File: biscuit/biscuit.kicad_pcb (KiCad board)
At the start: 2 copper layers, 45.7 x 45.7 mm, 47 parts, among them IC1 ATMEGA328-A, P1 D_IN, P2 PWR_IO, P3 UART, P4 ISP, P5 D_OUT, P6 MOT_1, P7 MOT_2, Q1 BC849, Q2 BC856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

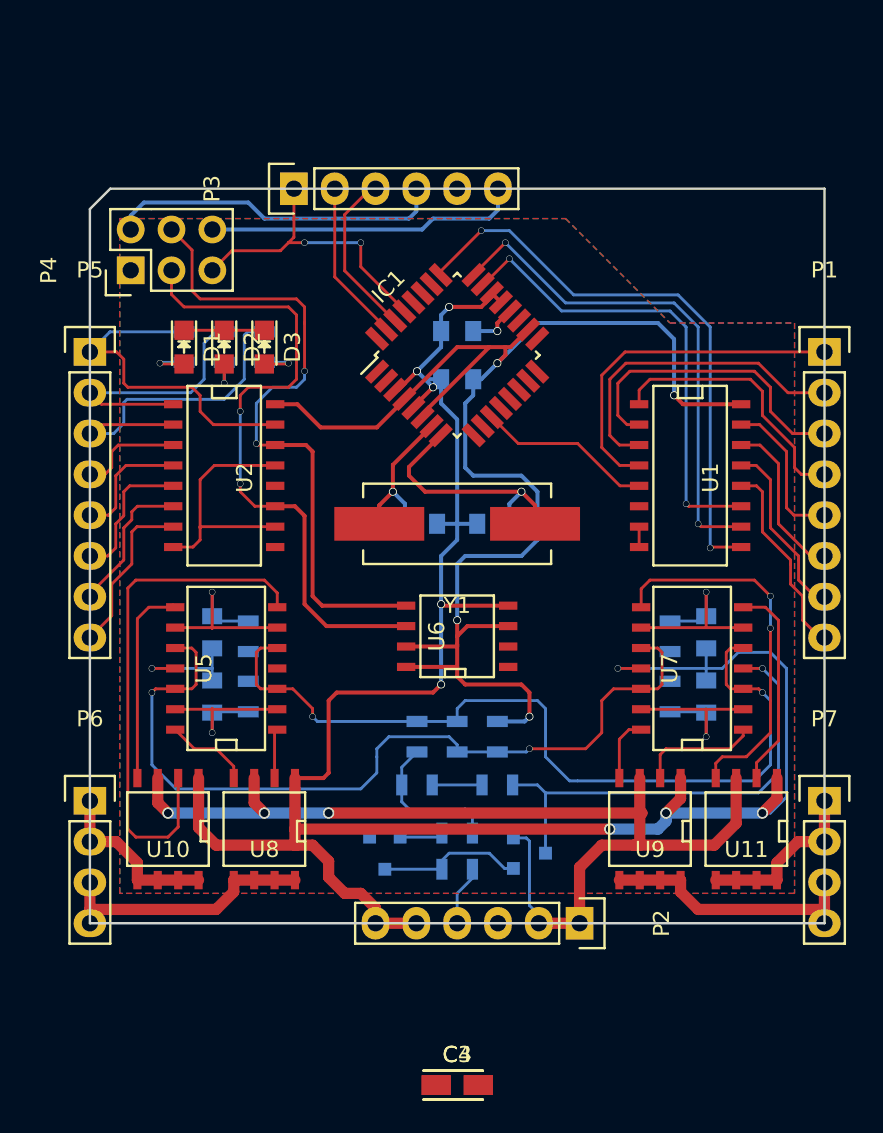
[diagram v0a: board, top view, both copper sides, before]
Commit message: First sucessful route for bisquit board
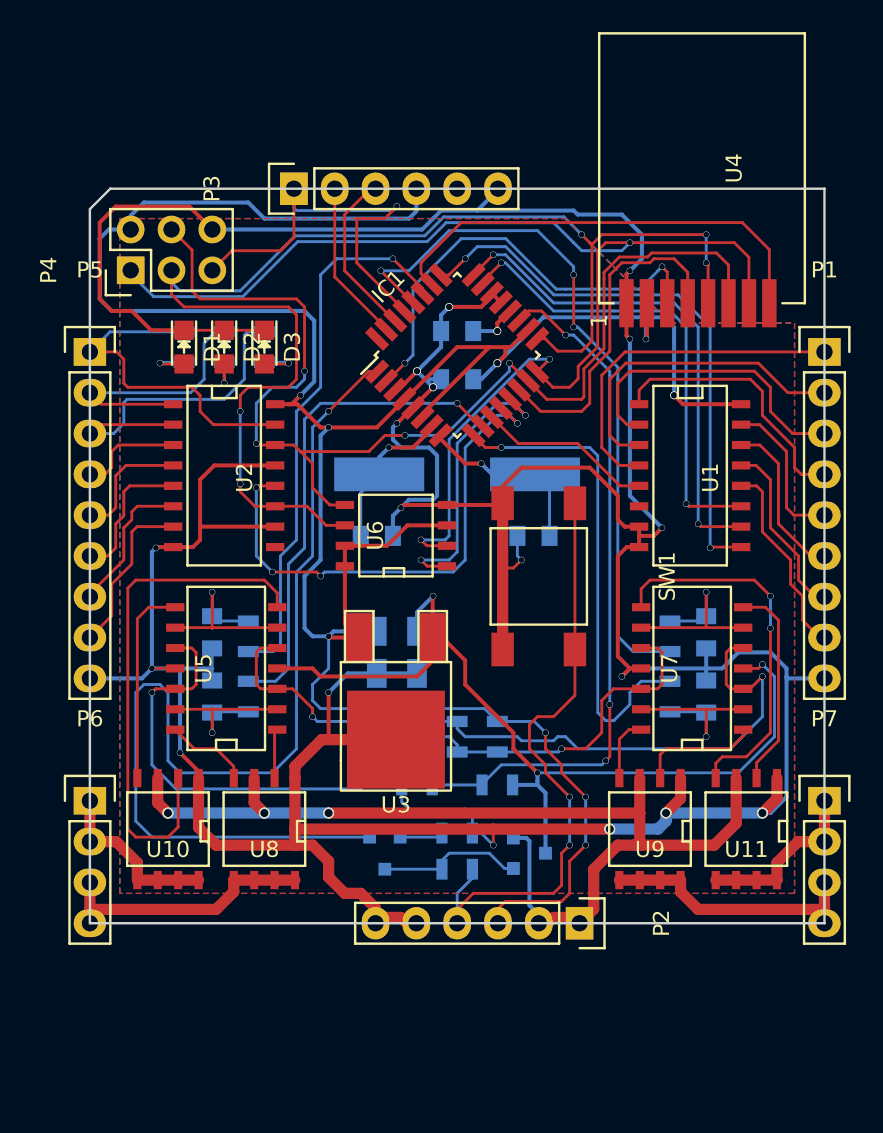
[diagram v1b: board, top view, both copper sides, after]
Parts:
- added SW1: SW_PWR, custom:Schurter_LSG_1301, F.Cu at (70.1, 61.3)
- added U3: TS2940CP33, TO_SOT_Packages_SMD:TO-252-2Lead, F.Cu at (61.2, 65.1)
- added U4: RFM75, custom:RFM75, F.Cu at (80.2, 35.9)
- C3, C4, Y1: moved to B.Cu
- P1, P5: footprint Pin_Headers:Pin_Header_Straight_1x08 -> Pin_Headers:Pin_Header_Straight_1x09
- moved C4 27.4 mm to (60.0, 66.0), turned to 270 degrees
- moved C3 27.1 mm to (62.5, 66.0), turned to 270 degrees
- moved U6 7.34 mm to (61.2, 58.7)
- moved Y1 3.08 mm to (65.0, 54.9)
- moved C5 2.85 mm to (60.0, 58.8)
- moved C6 2.61 mm to (69.8, 58.8)
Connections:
- IC1 pad 26: Net-(IC1-Pad26) -> /RF_IRQ
- IC1 pad 32: /RF_IRQ -> Net-(IC1-Pad32)
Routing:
- net GND: track 197.6 -> 301.9 mm, vias 10 -> 18
- net /MISO: track 0.00 -> 78.2 mm, vias 0 -> 3
- net /POWER_HOLD: track 0.00 -> 64.4 mm, vias 0 -> 1
- net +3V3: track 114.4 -> 169.4 mm, vias 4 -> 9
- net /STATIC_2: track 0.00 -> 44.8 mm, vias 0 -> 3
- net /SCK: track 40.7 -> 82.7 mm, vias 2 -> 5
- net /BAT_FB: track 3.10 -> 43.2 mm, vias 0 -> 3
- net /PWR_BTN_EXT: track 4.36 -> 39.1 mm, vias 0 -> 2
- net /STATIC_1: track 0.00 -> 34.2 mm, vias 0 -> 1
- net /SS_SIPO: track 0.00 -> 32.1 mm, vias 0 -> 4
- net /PWM_1: track 0.00 -> 30.8 mm, vias 0 -> 1
- net /PWM_2: track 0.00 -> 30.4 mm, vias 0 -> 1
- net /MOSI: track 41.2 -> 70.8 mm, vias 2 -> 4
- net /RF_IRQ: track 0.00 -> 28.4 mm
- net VCC: track 29.1 -> 57.0 mm, vias 1 -> 3
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
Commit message: Routing cleanup
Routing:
- net GND: track 301.9 -> 349.6 mm, vias 18 -> 20
- net /POWER_HOLD: track 64.4 -> 54.7 mm
- net +3V3: track 169.4 -> 177.1 mm
- net /~RESET: track 26.5 -> 20.5 mm, vias 1 -> 2
- net /DO_1: track 16.7 -> 21.7 mm
- net +BATT: track 64.6 -> 68.8 mm
- net Net-(U10-Pad2): track 32.7 -> 28.7 mm
- net /SCK: track 82.7 -> 86.0 mm
- net /V_THH: track 52.4 -> 49.2 mm
- net /MUX_IN: track 10.9 -> 13.4 mm
- net /PWR_BTN_EXT: track 39.1 -> 37.2 mm
- net /STATIC_2: track 44.8 -> 42.9 mm
- net Net-(P1-Pad6): track 10.2 -> 12.1 mm
- net /MUX_1: track 31.5 -> 32.8 mm
- net Net-(P1-Pad2): track 20.1 -> 18.8 mm
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
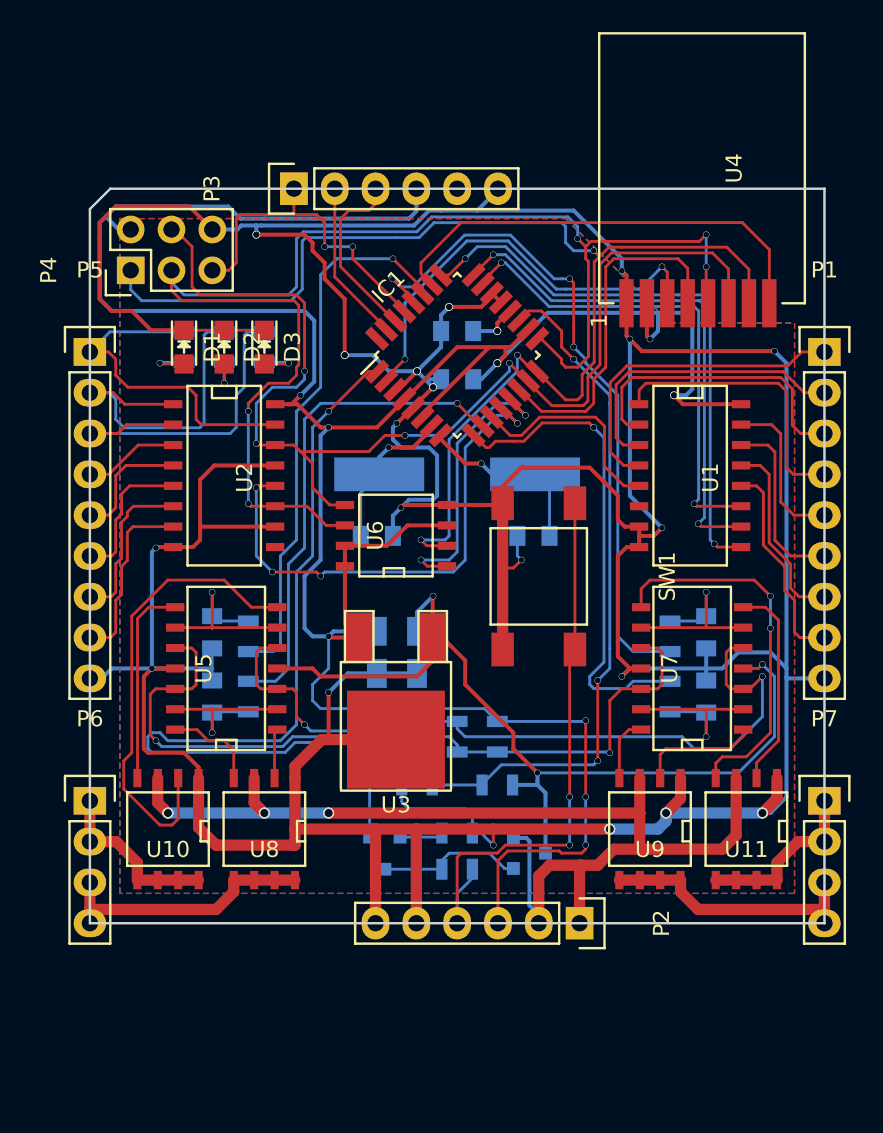
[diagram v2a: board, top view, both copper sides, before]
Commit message: Cleanup labels and add power LED
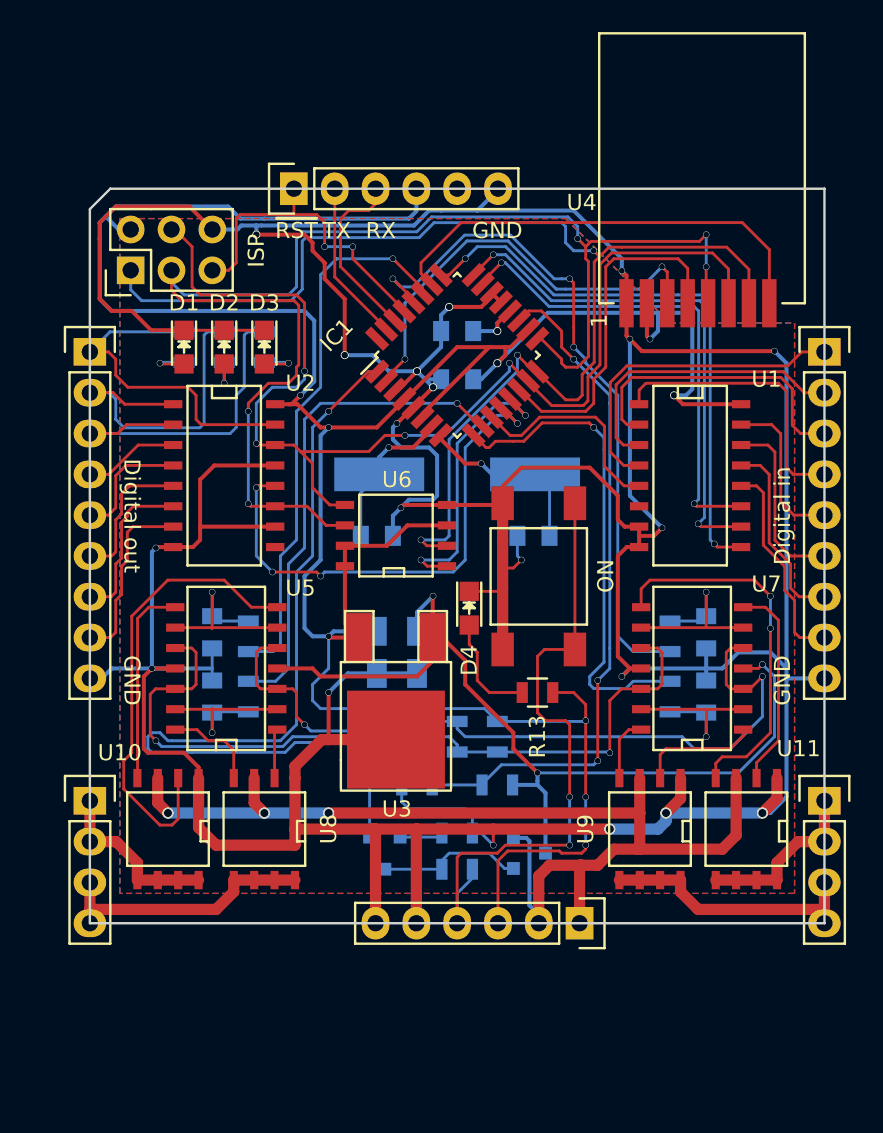
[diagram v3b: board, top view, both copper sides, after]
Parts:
- added D4: LED, LEDs:LED_0805, F.Cu at (65.8, 63.2)
- added R13: 1k, Resistors_SMD:R_0805, F.Cu at (70.0, 68.5)
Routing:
- net Net-(D4-Pad2): track 0.00 -> 6.77 mm
- net /PWR_BTN_EXT: track 37.2 -> 41.2 mm
- net +3V3: track 177.1 -> 180.4 mm
- net GND: track 349.6 -> 352.1 mm
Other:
- board text added: "Digital in"
- board text added: "Digital out"
- board text added: "GND"
- board text added: "ISP"
- board text added: "ON"
- board text added: "RX"
- board text added: "TX"
- board text added: "~RST"

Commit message: Added labels
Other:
- board text added: "BAT"
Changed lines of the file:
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@@
     (area 42.064999 37.064999 87.935001 82.935001)
     (thickness 1.6)
-    (drawings 15)
+    (drawings 17)
     (tracks 1131)
     (zones 0)
@@
     )
   )
+  (gr_text BAT (at 71.25 80.5) (layer F.SilkS)
+    (effects (font (size 1 1) (thickness 0.2)))
+  )
+  (gr_text GND (at 61.25 80.5) (layer F.SilkS)
+    (effects (font (size 1 1) (thickness 0.2)))
+  )
   (gr_text ON (at 74.25 61.25 90) (layer F.SilkS)
     (effects (font (size 1 1) (thickness 0.2)))
@@
   (gr_line (start 42.14 38.41) (end 43.41 37.14) (angle 90) (layer Edge.Cuts) (width 0.15))
   (segment (start 73 70.25) (end 73 69.25) (width 0.18) (layer F.Cu) (net 1))
-  (segment (start 72.25 68.5) (end 70.95 68.5) (width 0.18) (layer F.Cu) (net 1) (status 800000))
+  (segment (start 72.25 68.5) (end 70.95 68.5) (width 0.18) (layer F.Cu) (net 1))
   (segment (start 73 69.25) (end 72.25 68.5) (width 0.18) (layer F.Cu) (net 1))
   (segment (start 76.81 44.27) (end 76.81 46.31) (width 0.25) (layer F.Cu) (net 1))
@@
   (segment (start 68 47) (end 68.328427 47) (width 0.25) (layer F.Cu) (net 1))
   (segment (start 68.328427 47) (end 69.419417 45.90901) (width 0.25) (layer F.Cu) (net 1))
-  (segment (start 65.75 62.20098) (end 67.83 62.20098) (width 0.18) (layer F.Cu) (net 2) (status 400000))
+  (segment (start 65.75 62.20098) (end 67.83 62.20098) (width 0.18) (layer F.Cu) (net 2))
   (segment (start 68 62) (end 67.83 62) (width 0.18) (layer F.Cu) (net 2))
   (segment (start 68 62.03098) (end 68 62) (width 0.18) (layer F.Cu) (net 2))
@@
   (segment (start 69.5 77.75) (end 69.3 77.55) (width 0.25) (layer B.Cu) (net 42))
   (segment (start 69.5 81.75) (end 69.5 77.75) (width 0.25) (layer B.Cu) (net 42))
-  (segment (start 72.33 65.82) (end 70.43 65.82) (width 0.18) (layer F.Cu) (net 43) (status 400000))
+  (segment (start 72.33 65.82) (end 70.43 65.82) (width 0.18) (layer F.Cu) (net 43))
   (via (at 72 78) (size 0.4) (drill 0.36) (layers F.Cu B.Cu) (net 43))
   (segment (start 72 75) (end 72 78) (width 0.18) (layer B.Cu) (net 43))
@@
   (segment (start 75.69 70.81) (end 76.452 70.81) (width 0.18) (layer F.Cu) (net 71))
   (segment (start 75.095 71.405) (end 75.69 70.81) (width 0.18) (layer F.Cu) (net 71))
-  (segment (start 69.05 68.5) (end 67 68.5) (width 0.18) (layer F.Cu) (net 73) (status 400000))
-  (segment (start 65.75 65.5) (end 65.75 64.29902) (width 0.18) (layer F.Cu) (net 73) (status 800000))
+  (segment (start 69.05 68.5) (end 67 68.5) (width 0.18) (layer F.Cu) (net 73))
+  (segment (start 65.75 65.5) (end 65.75 64.29902) (width 0.18) (layer F.Cu) (net 73))
   (segment (start 66.25 66) (end 65.75 65.5) (width 0.18) (layer F.Cu) (net 73))
   (segment (start 66.25 67.75) (end 66.25 66) (width 0.18) (layer F.Cu) (net 73))

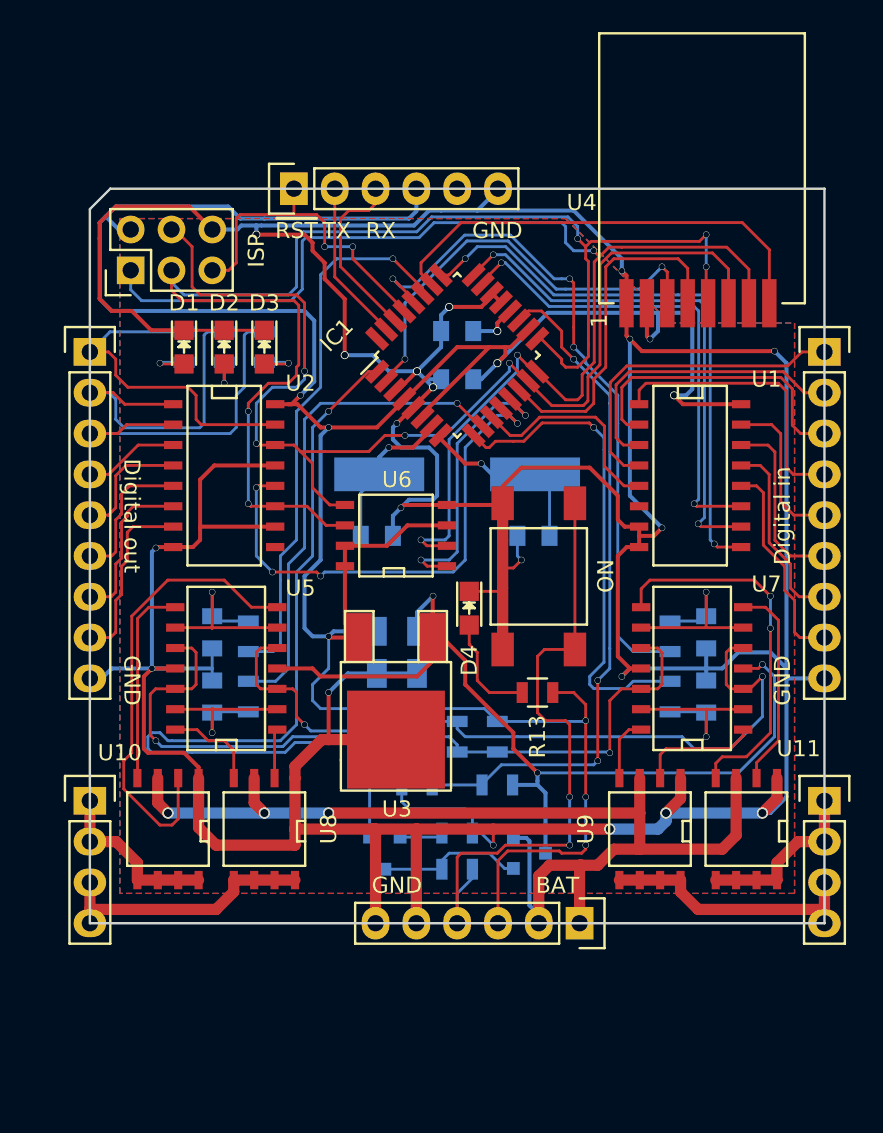
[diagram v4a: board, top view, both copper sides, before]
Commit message: Added reference to website
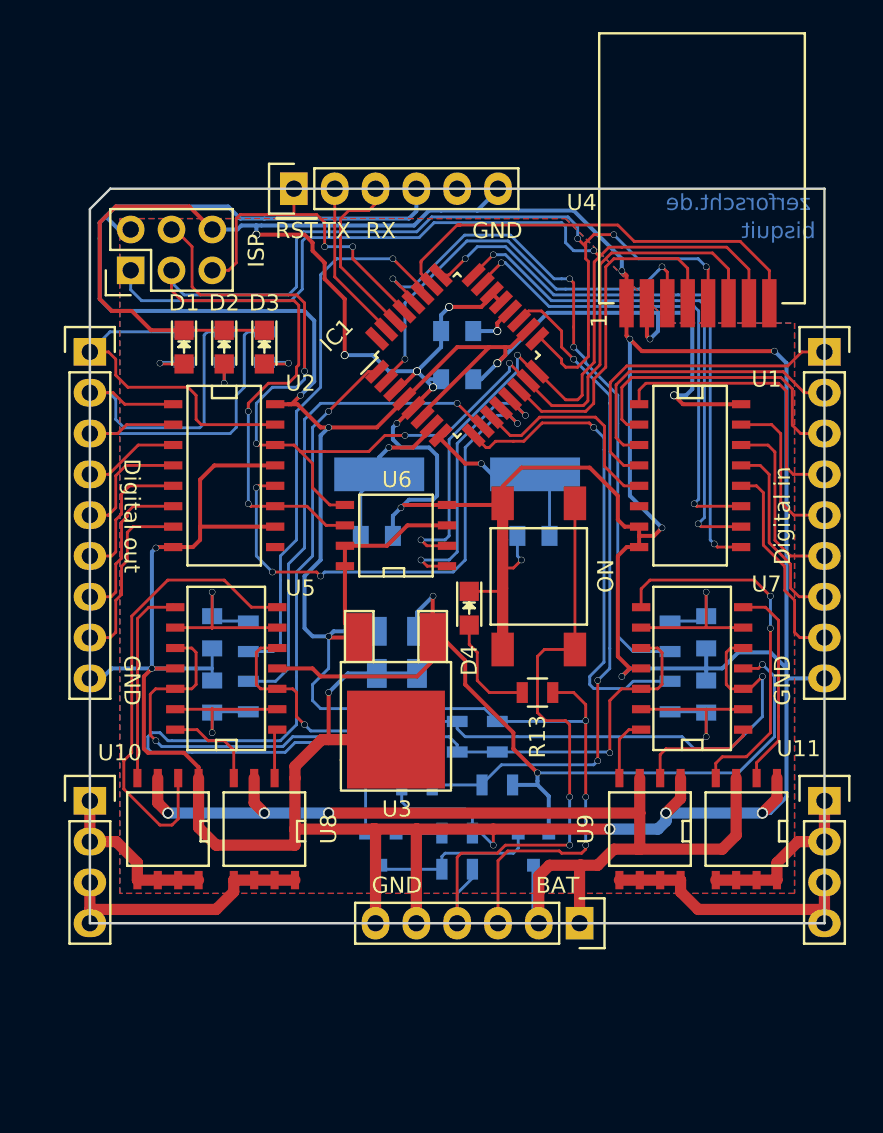
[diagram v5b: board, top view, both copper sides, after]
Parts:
- Q1: value BC849 -> Q_NPN_BEC
- Q2: value BC856 -> Q_PNP_BEC
- moved Q1 0.35 mm to (60.2, 78.2)
- moved Q2 0.35 mm to (69.8, 78.2), turned to 0 degrees
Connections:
- Q2 pad 2: +BATT -> VCC
- Q2 pad 3: VCC -> +BATT
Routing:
- net Net-(Q1-Pad3): track 9.13 -> 11.2 mm
- net +BATT: track 68.8 -> 67.1 mm
- net VCC: track 57.0 -> 55.8 mm
- net /SCK: track 86.0 -> 85.1 mm
- net /RF_IRQ: track 28.4 -> 27.7 mm
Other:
- board text added: "bisquit"
- board text added: "zerforscht.de"
